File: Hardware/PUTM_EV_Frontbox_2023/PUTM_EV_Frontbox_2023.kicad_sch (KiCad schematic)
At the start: 21 parts, among them J1 Conn_02x16_Counter_Clockwise, U1 LM4040C33FTA, U2 STM32G473RCTx

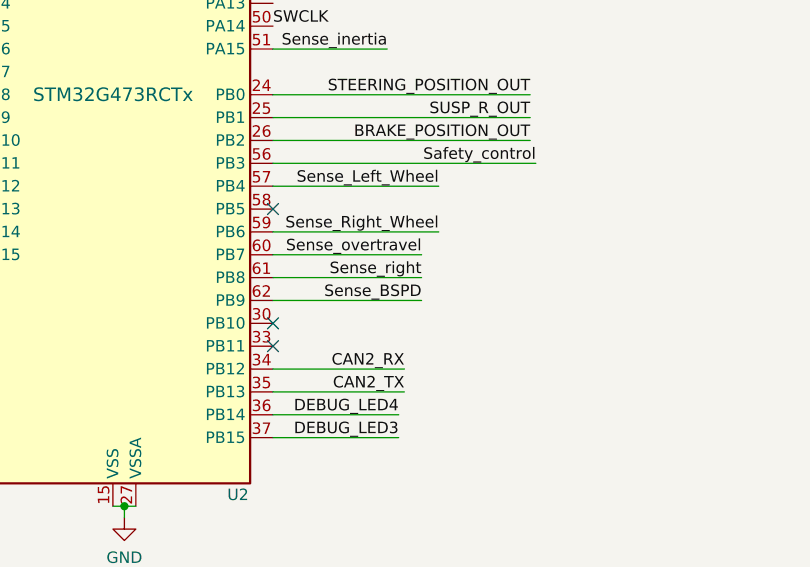
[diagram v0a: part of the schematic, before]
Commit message: Free PB0-Boot pin
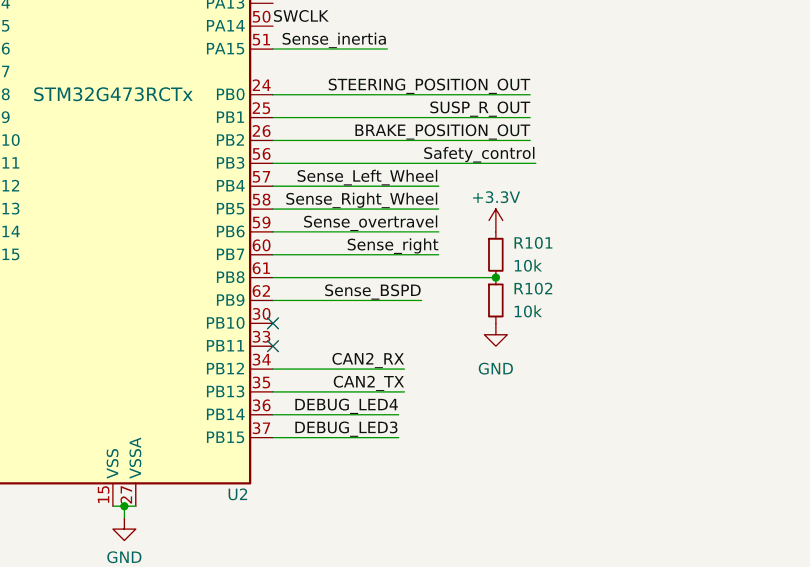
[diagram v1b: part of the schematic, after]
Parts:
- added R101, R102: 10k, Resistor_SMD:R_0603_1608Metric, symbol Device:R_Small
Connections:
- net +3.3V: now also R101.1
- net GND: now also R102.2
- net Sense_Right_Wheel: now also U2.58 (PB5); no longer U2.59 (PB6)
- net Sense_overtravel: now also U2.59 (PB6); no longer U2.60 (PB7)
- net Sense_right: now also U2.60 (PB7); no longer U2.61 (PB8)
- new net: R101.2, R102.1, U2.61 (PB8)
- no-connect marks 15 -> 14
